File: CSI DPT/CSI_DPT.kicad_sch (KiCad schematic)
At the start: 0 parts

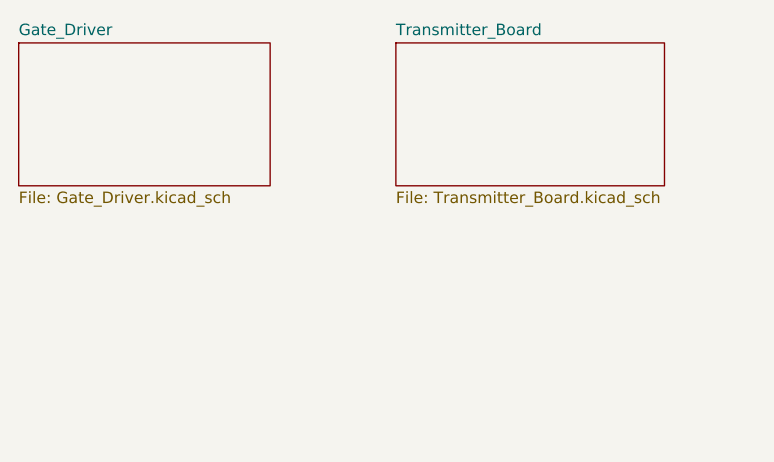
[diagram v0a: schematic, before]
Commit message: Gate Driver Complete
1. Competed half bridge gate driver
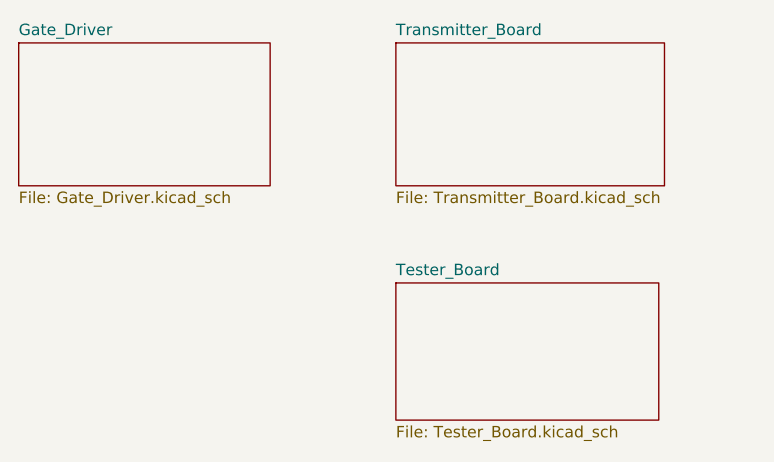
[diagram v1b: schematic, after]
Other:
- added sheet Tester_Board (Tester_Board.kicad_sch)
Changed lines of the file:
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@@
 	(paper "A4")
+	(sheet
+		(at 73.66 60.96)
+		(size 29.21 15.24)
+		(exclude_from_sim no)
+		(in_bom yes)
+		(on_board yes)
+		(dnp no)
+		(fields_autoplaced yes)
+		(stroke
+			(width 0.1524)
+			(type solid)
+		)
+		(fill
+			(color 0 0 0 0.0000)
+		)
+		(property "Sheetname" "Tester_Board"
+			(at 73.66 60.2484 0)
+			(effects
+				(font
+					(size 1.27 1.27)
+				)
+				(justify left bottom)
+			)
+		)
+		(property "Sheetfile" "Tester_Board.kicad_sch"
+			(at 73.66 76.7846 0)
+			(effects
+				(font
+					(size 1.27 1.27)
+				)
+				(justify left top)
+			)
+		)
+		(instances
+			(project "CSI_DPT"
+				(path "/73752a49-eb43-43a5-aaa4-eec4feca9056"
+					(page "4")
+				)
+			)
+		)
+	)
 	(sheet
 		(at 31.75 34.29)

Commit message: test commit
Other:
- sheet Gate_Driver ports: added VGATE_H, VGATE_L, VSOURCE_H, VSOURCE_L; removed none
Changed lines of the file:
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@@
+			)
+		)
+		(pin "VGATE_H" output
+			(at 59.69 36.83 0)
+			(effects
+				(font
+					(size 1.27 1.27)
+				)
+				(justify right)
+			)
+		)
+		(pin "VGATE_L" output
+			(at 59.69 44.45 0)
+			(effects
+				(font
+					(size 1.27 1.27)
+				)
+				(justify right)
+			)
+		)
+		(pin "VSOURCE_H" output
+			(at 59.69 39.37 0)
+			(effects
+				(font
+					(size 1.27 1.27)
+				)
+				(justify right)
+			)
+		)
+		(pin "VSOURCE_L" output
+			(at 59.69 46.99 0)
+			(effects
+				(font
+					(size 1.27 1.27)
+				)
+				(justify right)
 			)
 		)
